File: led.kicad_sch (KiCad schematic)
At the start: 11 parts, among them U4 C5944

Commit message: Footprint fix, preliminary pcb
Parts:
- U4: footprint (none) -> Package_SO:TSSOP-20_4.4x6.5mm_P0.65mm
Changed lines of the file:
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@@
       (effects (font (size 1.27 1.27)) (justify left))
     )
-    (property "Footprint" "" (at 95.25 87.63 0)
+    (property "Footprint" "Package_SO:TSSOP-20_4.4x6.5mm_P0.65mm" (at 95.25 87.63 0)
       (effects (font (size 1.27 1.27)) hide)
     )

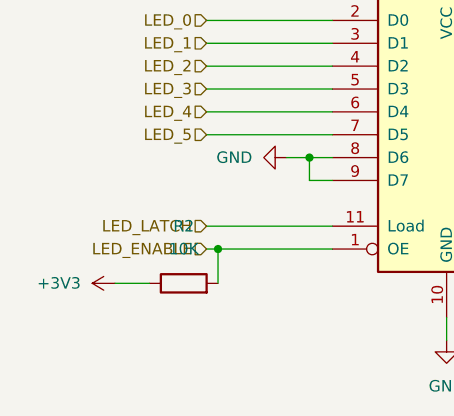
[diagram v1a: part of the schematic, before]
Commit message: Added JLPCB DRCs, antenna hatching
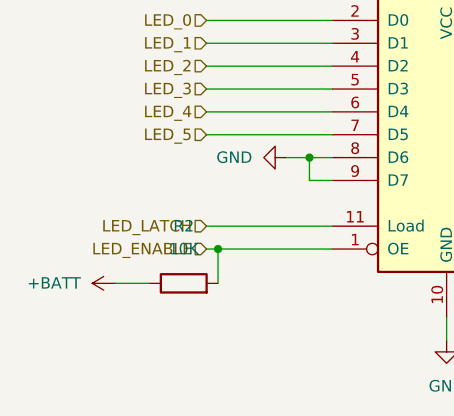
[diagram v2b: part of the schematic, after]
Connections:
- net +3V3 is gone; now on net +BATT: R2.1
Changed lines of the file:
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@@
+    )
+  )
+  (symbol (lib_id "power:+BATT") (at 58.42 104.14 90) (unit 1)
+    (in_bom yes) (on_board yes) (dnp no) (fields_autoplaced)
+    (property "Reference" "#PWR024" (at 62.23 104.14 0)
+      (effects (font (size 1.27 1.27)) hide)
+    )
+    (property "Value" "+BATT" (at 54.61 104.14 90)
+      (effects (font (size 1.27 1.27)) (justify left))
+    )
+    (property "Footprint" "" (at 58.42 104.14 0)
+      (effects (font (size 1.27 1.27)) hide)
+    )
+    (property "Datasheet" "" (at 58.42 104.14 0)
+      (effects (font (size 1.27 1.27)) hide)
+    )
+    (pin "1")
+    (instances
+      (project "reaction-trainer"
+        (path "/726cb70d-0185-4970-973b-037545fc3942/1b834bb3-86eb-409b-9f04-1d08416824c1"
+          (reference "#PWR024") (unit 1)
+        )
+      )
     )
   )
@@
         )
       )
-    )
-  )
-  (symbol (lib_id "power:+3V3") (at 58.42 104.14 90) (unit 1)
-    (in_bom yes) (on_board yes) (dnp no) (fields_autoplaced)
-    (property "Reference" "#PWR045" (at 62.23 104.14 0)
-      (effects (font (size 1.27 1.27)) hide)
-    )
-    (property "Value" "+3V3" (at 54.61 104.14 90)
-      (effects (font (size 1.27 1.27)) (justify left))
-    )
-    (property "Footprint" "" (at 58.42 104.14 0)
-      (effects (font (size 1.27 1.27)) hide)
-    )
-    (property "Datasheet" "" (at 58.42 104.14 0)
-      (effects (font (size 1.27 1.27)) hide)
-    )
-    (pin "1")
-    (instances
-      (project "reaction-trainer"
-        (path "/726cb70d-0185-4970-973b-037545fc3942/1b834bb3-86eb-409b-9f04-1d08416824c1"
-          (reference "#PWR045") (unit 1)
-        )
-      )

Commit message: Field updates, generating fab files
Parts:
- C7: value 0.1uF -> 0.1uF 20%; JLCPCB Part # (none) -> C359190
- D1, D2: JLCPCB Part # (none) -> C784541
- R10, R8: value 30 -> 30 5% 125mW; JLCPCB Part # (none) -> C2930273
- R11, R6, R7, R9: value 15 -> 15 5% 125mW; JLCPCB Part # (none) -> C2930246
- R2: value 10K -> 10K 5%; JLCPCB Part # (none) -> C2906885
- U4: value C5944 -> 74HC573PW,118; JLCPCB Part # (none) -> C5944
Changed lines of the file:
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@@
       (effects (font (size 1.27 1.27)) (justify left))
     )
-    (property "Value" "C5944" (at 97.2059 69.85 0)
+    (property "Value" "74HC573PW,118" (at 97.2059 69.85 0)
       (effects (font (size 1.27 1.27)) (justify left))
     )
@@
     )
     (property "Datasheet" "74xx/74hc573.pdf" (at 95.25 87.63 0)
+      (effects (font (size 1.27 1.27)) hide)
+    )
+    (property "JLCPCB Part #" "C5944" (at 95.25 87.63 0)
       (effects (font (size 1.27 1.27)) hide)
     )
@@
       (effects (font (size 1.27 1.27)) hide)
     )
-    (property "Datasheet" "~" (at 152.4 102.87 0)
+    (property "Datasheet" "https://www.lcsc.com/product-detail/Light-Emitting-Diodes-LED_TCWIN-TC5050RGBF20-3CES-AF51_C784541.html" (at 152.4 102.87 0)
+      (effects (font (size 1.27 1.27)) hide)
+    )
+    (property "JLCPCB Part #" "C784541" (at 152.4 101.6 0)
       (effects (font (size 1.27 1.27)) hide)
     )
@@
       (effects (font (size 1.27 1.27)))
     )
-    (property "Value" "15" (at 138.43 78.74 90)
+    (property "Value" "15 5% 125mW" (at 138.43 78.74 90)
       (effects (font (size 1.27 1.27)))
     )
@@
       (effects (font (size 1.27 1.27)) hide)
     )
-    (property "Datasheet" "~" (at 138.43 82.55 0)
+    (property "Datasheet" "https://www.lcsc.com/product-detail/Chip-Resistor-Surface-Mount_FOJAN-FRC0805J150TS_C2930246.html" (at 138.43 82.55 0)
+      (effects (font (size 1.27 1.27)) hide)
+    )
+    (property "JLCPCB Part #" "C2930246" (at 138.43 82.55 0)
       (effects (font (size 1.27 1.27)) hide)
     )
@@
       (effects (font (size 1.27 1.27)))
     )
-    (property "Value" "30" (at 138.43 97.79 90)
+    (property "Value" "30 5% 125mW" (at 138.43 97.79 90)
       (effects (font (size 1.27 1.27)))
     )
@@
       (effects (font (size 1.27 1.27)) hide)
     )
-    (property "Datasheet" "~" (at 138.43 101.6 0)
+    (property "Datasheet" "https://www.lcsc.com/product-detail/Chip-Resistor-Surface-Mount_FOJAN-FRC0805J300TSD_C2930273.html" (at 138.43 101.6 0)
+      (effects (font (size 1.27 1.27)) hide)
+    )
+    (property "JLCPCB Part #" "C2930273" (at 138.43 101.6 0)
       (effects (font (size 1.27 1.27)) hide)
     )
@@
       (effects (font (size 1.27 1.27)))
     )
-    (property "Value" "0.1uF" (at 104.14 69.85 90)
+    (property "Value" "0.1uF 20%" (at 104.14 69.85 90)
       (effects (font (size 1.27 1.27)))
     )
@@
       (effects (font (size 1.27 1.27)) hide)
     )
-    (property "Datasheet" "~" (at 104.14 64.77 0)
+    (property "Datasheet" "https://www.lcsc.com/product-detail/Multilayer-Ceramic-Capacitors-MLCC-SMD-SMT_CCTC-TCC0402X5R104M250AT_C359190.html" (at 104.14 64.77 0)
+      (effects (font (size 1.27 1.27)) hide)
+    )
+    (property "JLCPCB Part #" "C359190" (at 104.14 64.77 0)
       (effects (font (size 1.27 1.27)) hide)
     )
@@
       (effects (font (size 1.27 1.27)) hide)
     )
-    (property "Datasheet" "~" (at 152.4 78.74 0)
+    (property "Datasheet" "https://www.lcsc.com/product-detail/Light-Emitting-Diodes-LED_TCWIN-TC5050RGBF20-3CES-AF51_C784541.html" (at 152.4 78.74 0)
+      (effects (font (size 1.27 1.27)) hide)
+    )
+    (property "JLCPCB Part #" "C784541" (at 152.4 77.47 0)
       (effects (font (size 1.27 1.27)) hide)
     )
@@
       (effects (font (size 1.27 1.27)))
     )
-    (property "Value" "30" (at 138.43 73.66 90)
+    (property "Value" "30 5% 125mW" (at 138.43 73.66 90)
       (effects (font (size 1.27 1.27)))
     )
@@
       (effects (font (size 1.27 1.27)) hide)
     )
-    (property "Datasheet" "~" (at 138.43 77.47 0)
+    (property "Datasheet" "https://www.lcsc.com/product-detail/Chip-Resistor-Surface-Mount_FOJAN-FRC0805J300TSD_C2930273.html" (at 138.43 77.47 0)
+      (effects (font (size 1.27 1.27)) hide)
+    )
+    (property "JLCPCB Part #" "C2930273" (at 138.43 77.47 0)
       (effects (font (size 1.27 1.27)) hide)
     )
@@
       (effects (font (size 1.27 1.27)))
     )
-    (property "Value" "15" (at 138.43 102.87 90)
+    (property "Value" "15 5% 125mW" (at 138.43 102.87 90)
       (effects (font (size 1.27 1.27)))
     )
@@
       (effects (font (size 1.27 1.27)) hide)
     )
-    (property "Datasheet" "~" (at 138.43 106.68 0)
+    (property "Datasheet" "https://www.lcsc.com/product-detail/Chip-Resistor-Surface-Mount_FOJAN-FRC0805J150TS_C2930246.html" (at 138.43 106.68 0)
+      (effects (font (size 1.27 1.27)) hide)
+    )
+    (property "JLCPCB Part #" "C2930246" (at 138.43 106.68 0)
       (effects (font (size 1.27 1.27)) hide)
     )
@@
       (effects (font (size 1.27 1.27)))
     )
-    (property "Value" "15" (at 138.43 68.58 90)
+    (property "Value" "15 5% 125mW" (at 138.43 68.58 90)
       (effects (font (size 1.27 1.27)))
     )
@@
       (effects (font (size 1.27 1.27)) hide)
     )
-    (property "Datasheet" "~" (at 138.43 72.39 0)
+    (property "Datasheet" "https://www.lcsc.com/product-detail/Chip-Resistor-Surface-Mount_FOJAN-FRC0805J150TS_C2930246.html" (at 138.43 72.39 0)
+      (effects (font (size 1.27 1.27)) hide)
+    )
+    (property "JLCPCB Part #" "C2930246" (at 138.43 72.39 0)
       (effects (font (size 1.27 1.27)) hide)
     )
@@
       (effects (font (size 1.27 1.27)))
     )
-    (property "Value" "15" (at 138.43 92.71 90)
+    (property "Value" "15 5% 125mW" (at 138.43 92.71 90)
       (effects (font (size 1.27 1.27)))
     )
@@
       (effects (font (size 1.27 1.27)) hide)
     )
-    (property "Datasheet" "~" (at 138.43 96.52 0)
+    (property "Datasheet" "https://www.lcsc.com/product-detail/Chip-Resistor-Surface-Mount_FOJAN-FRC0805J150TS_C2930246.html" (at 138.43 96.52 0)
+      (effects (font (size 1.27 1.27)) hide)
+    )
+    (property "JLCPCB Part #" "C2930246" (at 138.43 96.52 0)
       (effects (font (size 1.27 1.27)) hide)
     )
@@
       (effects (font (size 1.27 1.27)))
     )
-    (property "Value" "10K" (at 66.04 100.33 90)
+    (property "Value" "10K 5%" (at 66.04 100.33 90)
       (effects (font (size 1.27 1.27)))
     )
@@
       (effects (font (size 1.27 1.27)) hide)
     )
-    (property "Datasheet" "~" (at 66.04 104.14 0)
-      (effects (font (size 1.27 1.27)) hide)
-    )
+    (property "Datasheet" "https://www.lcsc.com/product-detail/Chip-Resistor-Surface-Mount_FOJAN-FRC0402J103-TS_C2906885.html" (at 66.04 104.14 0)
+      (effects (font (size 1.27 1.27)) hide)
+    )
+    (property "JLCPCB Part #" "C2906885" (at 66.04 104.14 0)
+      (effects (font (size 1.27 1.27)) hide)
+    )

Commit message: Changed outline for DFM
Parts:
- C7: JLCPCB Part # C359190 -> (none); LCSC (none) -> C359190
- D1, D2: JLCPCB Part # C784541 -> (none); LCSC (none) -> C784541
- R10, R8: JLCPCB Part # C2930273 -> (none); LCSC (none) -> C2930273
- R11, R6, R7, R9: JLCPCB Part # C2930246 -> (none); LCSC (none) -> C2930246
- R2: JLCPCB Part # C2906885 -> (none); LCSC (none) -> C2906885
- U4: JLCPCB Part # C5944 -> (none); LCSC (none) -> C5944
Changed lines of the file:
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@@
       (effects (font (size 1.27 1.27)) hide)
     )
-    (property "JLCPCB Part #" "C5944" (at 95.25 87.63 0)
+    (property "LCSC" "C5944" (at 95.25 87.63 0)
       (effects (font (size 1.27 1.27)) hide)
     )
@@
       (effects (font (size 1.27 1.27)) hide)
     )
-    (property "JLCPCB Part #" "C784541" (at 152.4 101.6 0)
+    (property "LCSC" "C784541" (at 152.4 101.6 0)
       (effects (font (size 1.27 1.27)) hide)
     )
@@
       (effects (font (size 1.27 1.27)) hide)
     )
-    (property "JLCPCB Part #" "C2930246" (at 138.43 82.55 0)
+    (property "LCSC" "C2930246" (at 138.43 82.55 0)
       (effects (font (size 1.27 1.27)) hide)
     )
@@
       (effects (font (size 1.27 1.27)) hide)
     )
-    (property "JLCPCB Part #" "C2930273" (at 138.43 101.6 0)
+    (property "LCSC" "C2930273" (at 138.43 101.6 0)
       (effects (font (size 1.27 1.27)) hide)
     )
@@
       (effects (font (size 1.27 1.27)) hide)
     )
-    (property "JLCPCB Part #" "C359190" (at 104.14 64.77 0)
+    (property "LCSC" "C359190" (at 104.14 64.77 0)
       (effects (font (size 1.27 1.27)) hide)
     )
@@
       (effects (font (size 1.27 1.27)) hide)
     )
-    (property "JLCPCB Part #" "C784541" (at 152.4 77.47 0)
+    (property "LCSC" "C784541" (at 152.4 77.47 0)
       (effects (font (size 1.27 1.27)) hide)
     )
@@
       (effects (font (size 1.27 1.27)) hide)
     )
-    (property "JLCPCB Part #" "C2930273" (at 138.43 77.47 0)
+    (property "LCSC" "C2930273" (at 138.43 77.47 0)
       (effects (font (size 1.27 1.27)) hide)
     )
@@
       (effects (font (size 1.27 1.27)) hide)
     )
-    (property "JLCPCB Part #" "C2930246" (at 138.43 106.68 0)
+    (property "LCSC" "C2930246" (at 138.43 106.68 0)
       (effects (font (size 1.27 1.27)) hide)
     )
@@
       (effects (font (size 1.27 1.27)) hide)
     )
-    (property "JLCPCB Part #" "C2930246" (at 138.43 72.39 0)
+    (property "LCSC" "C2930246" (at 138.43 72.39 0)
       (effects (font (size 1.27 1.27)) hide)
     )
@@
       (effects (font (size 1.27 1.27)) hide)
     )
-    (property "JLCPCB Part #" "C2930246" (at 138.43 96.52 0)
+    (property "LCSC" "C2930246" (at 138.43 96.52 0)
       (effects (font (size 1.27 1.27)) hide)
     )
@@
       (effects (font (size 1.27 1.27)) hide)
     )
-    (property "JLCPCB Part #" "C2906885" (at 66.04 104.14 0)
-      (effects (font (size 1.27 1.27)) hide)
-    )
+    (property "LCSC" "C2906885" (at 66.04 104.14 0)
+      (effects (font (size 1.27 1.27)) hide)
+    )
